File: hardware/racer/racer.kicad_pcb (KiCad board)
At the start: 4 copper layers, 36 x 50.2 mm, 83 parts, among them J1 motor0, J11 UART, J12 JST 2.0 BATT, J2 motor1, J3 motor0, J4 motor1, J5 motor0, J6 motor1, J7 motor0, J8 motor1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

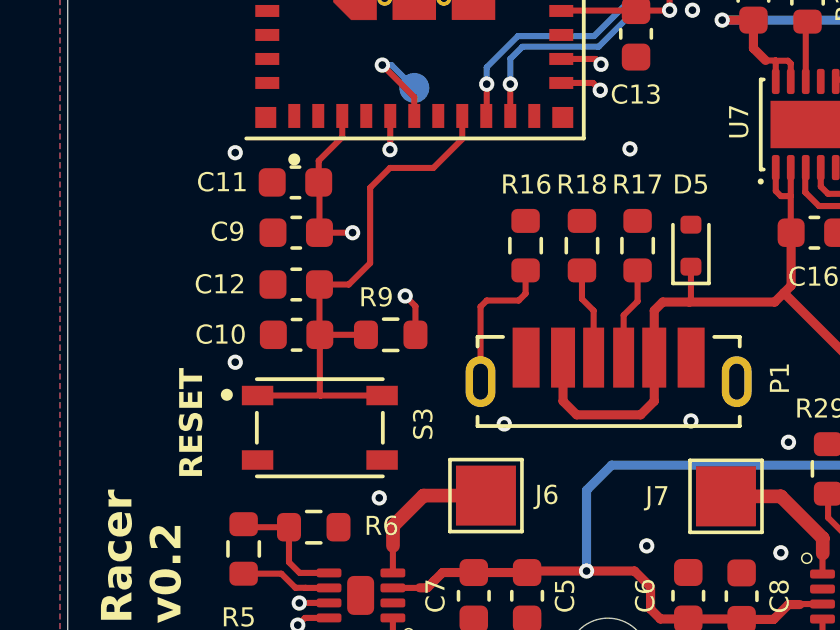
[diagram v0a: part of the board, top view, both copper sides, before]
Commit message: Schematic improvement & LCSC BOM
- Schematic readability improvements.
- Changed schematic symbols.
- Changed to hierarchical schematic.
- Added LCSC BOM for the available components.
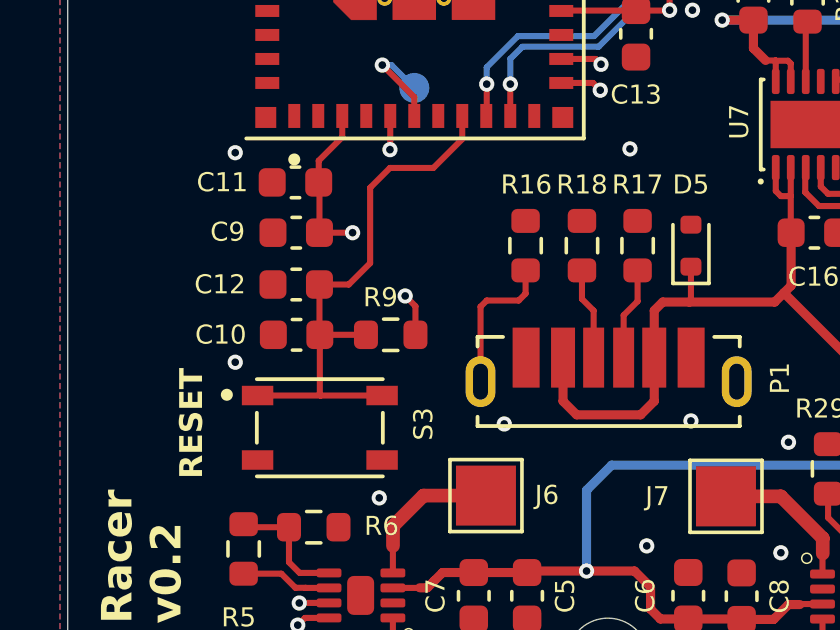
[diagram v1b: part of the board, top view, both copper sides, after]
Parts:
- C10: value 1uF 25V -> 1uF
- C11, C12, C13, C3, C4, C7, C8: value 0.1uF -> 100nF
- J9: value Conn_02x03_SMT -> Conn_02x03
- R16: value 1M -> 1Meg
- R17, R18: value 5k1 -> 5.1k
- R22: value 1.43K -> 5k
- R23: value 1.43K -> 1.43k
- R24: value 75K -> 75k
- S2, S3: value TL4100AF240QG_ -> TL4100AF240QG
- TH1: value TH 10k -> 10k
- turned R9 to 0 degrees
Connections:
- net /ADC_BATT renamed /MCU/ADC_BATT
- net /CHRGR+ renamed Net-(C17-Pad1)
- net /HAL_OUT renamed /MCU/HAL_OUT
- net /OPT_INT renamed /MCU/OPT_INT
- net /SCL renamed /MCU/SCL
- net /SDA renamed /MCU/SDA
- net /STAT1 renamed Net-(D9-K)
- net /STAT2 renamed Net-(D8-K)
- net /U0RXD renamed /MCU/U0_{RXD}
- net /U0TXD renamed /MCU/U0_{TXD}
- net MOTOR_0_IN1 renamed MOTOR_{0_{IN1}}
- net MOTOR_0_IN2 renamed MOTOR_{0_{IN2}}
- net MOTOR_1_IN1 renamed MOTOR_{1_{IN1}}
- net MOTOR_1_IN2 renamed MOTOR_{1_{IN2}}
- net Net-(U5-IO08) renamed /MCU/Boot_opt
- net Net-(U5-IO9) renamed /MCU/Boot
- C10 pad 1: /CP_EN -> /MCU/Enable
- C12 pad 1: /CP_EN -> /MCU/Enable
- C13 pad 1: +3V3 -> Net-(U5A-VBAT)
- D5 pad 1: +5V -> GND
- D5 pad 2: GND -> +5V
- R23 pad 1: Net-(R23-Pad1) -> Net-(U7-THERM)
- R23 pad 2: Net-(U7-THERM) -> Net-(R23-Pad2)
- R24 pad 1: GND -> Net-(R23-Pad2)
- R24 pad 2: Net-(R23-Pad1) -> GND
- R25 pad 1: Net-(D6-A) -> RAW
- R25 pad 2: RAW -> Net-(D6-A)
- R9 pad 1: +3V3 -> /MCU/Enable
- R9 pad 2: /CP_EN -> +3V3
- S3 pad 1: /CP_EN -> /MCU/Enable
- TH1 pad 1: Net-(R23-Pad1) -> Net-(R23-Pad2)
- U3 pad 1: Net-(J5-Pin_1) -> Net-(J6-Pin_1)
- U3 pad 4: Net-(J6-Pin_1) -> Net-(J5-Pin_1)
- U4 pad 1: Net-(J7-Pin_1) -> Net-(J8-Pin_1)
- U4 pad 4: Net-(J8-Pin_1) -> Net-(J7-Pin_1)
- U5 pad 15: +3V3 -> Net-(U5A-VBAT)
- U5 pad 17: unconnected-(U5-NC-Pad17) -> (no net)
- U5 pad 28: unconnected-(U5-NC-Pad28) -> (no net)
- U5 pad 29: unconnected-(U5-NC-Pad29) -> (no net)
- U5 pad 32: unconnected-(U5-NC-Pad32) -> (no net)
- U5 pad 33: unconnected-(U5-NC-Pad33) -> (no net)
- U5 pad 34: unconnected-(U5-NC-Pad34) -> (no net)
- U5 pad 35: unconnected-(U5-NC-Pad35) -> (no net)
- U5 pad 4: unconnected-(U5-NC-Pad4) -> (no net)
- U5 pad 7: unconnected-(U5-NC-Pad7) -> (no net)
- U5 pad 8: /CP_EN -> /MCU/Enable
- U6 pad 2: GND -> (no net)
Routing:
- net /MCU/Enable: track 0.00 -> 18.4 mm
- net /CP_EN: track 18.4 -> 0.00 mm
- net Net-(R23-Pad1): track 3.45 -> 0.00 mm
- net (no net): track 0.00 -> 3.45 mm
